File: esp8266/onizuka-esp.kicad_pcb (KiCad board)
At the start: 2 copper layers, 49 x 19 mm, 7 parts, among them P1 FTDI, U1 ESP-01, U2 ESP-12E

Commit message: More faffing
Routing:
- net GND: vias 2 -> 6
- added copper zone on F.Cu, net GND
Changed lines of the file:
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@@
     (thickness 1.6)
     (drawings 4)
-    (tracks 80)
+    (tracks 84)
     (zones 0)
     (modules 7)
@@
       (effects (font (size 1 1) (thickness 0.15)))
     )
-    (fp_text value 100n (at -3.302 0 90) (layer F.SilkS)
+    (fp_text value 100n (at 3.3655 0 90) (layer F.SilkS)
       (effects (font (size 1 1) (thickness 0.15)))
     )
@@
       (effects (font (size 1 1) (thickness 0.15)))
     )
-    (fp_text value FTDI (at 11.41 -1.988 270) (layer F.SilkS)
+    (fp_text value FTDI (at 11.6205 -1.9685 270) (layer F.SilkS) hide
       (effects (font (size 1 1) (thickness 0.15)))
     )
@@
       (effects (font (size 1 1) (thickness 0.15)))
     )
-    (fp_text value 22u (at -2.794 0 90) (layer F.SilkS)
+    (fp_text value 22u (at 2.8575 0.0635 90) (layer F.SilkS)
       (effects (font (size 1 1) (thickness 0.15)))
     )
@@
       (effects (font (size 1 1) (thickness 0.15)))
     )
-    (fp_text value ESP-01 (at 3.81 -1.9685 450) (layer F.SilkS)
+    (fp_text value ESP-01 (at 6.477 4.953 450) (layer F.SilkS)
       (effects (font (size 1 1) (thickness 0.15)))
     )
@@
       (scale (xyz 1 1 1))
       (rotate (xyz 0 0 180))
+    )
+    (model ./esp-01.wrl
+      (at (xyz 0.15 -0.05 0.34))
+      (scale (xyz 1 1 1))
+      (rotate (xyz 0 0 0))
     )
   )
@@
   (gr_line (start 69 37.5) (end 20 37.5) (angle 90) (layer Edge.Cuts) (width 0.15))
   (gr_line (start 69 18.5) (end 69 37.5) (angle 90) (layer Edge.Cuts) (width 0.15))
-  (segment (start 57.9635 32.1945) (end 57.9635 33.7185) (width 0.25) (layer F.Cu) (net 1) (status C00000))
-  (segment (start 57.9635 33.7185) (end 57.9635 32.9685) (width 0.25) (layer F.Cu) (net 1) (status 400000))
+  (via (at 35.5 30) (size 0.6) (drill 0.4) (layers F.Cu B.Cu) (net 1))
+  (via (at 44 21.5) (size 0.6) (drill 0.4) (layers F.Cu B.Cu) (net 1))
+  (via (at 36.5 33.5) (size 0.6) (drill 0.4) (layers F.Cu B.Cu) (net 1))
+  (via (at 52 31) (size 0.6) (drill 0.4) (layers F.Cu B.Cu) (net 1))
+  (segment (start 57.9635 32.1945) (end 57.9635 33.7185) (width 0.25) (layer F.Cu) (net 1))
+  (segment (start 57.9635 33.7185) (end 57.9635 32.9685) (width 0.25) (layer F.Cu) (net 1))
   (segment (start 57.9635 32.9685) (end 57.9755 32.9565) (width 0.25) (layer F.Cu) (net 1))
   (via (at 57.9755 32.9565) (size 0.6) (drill 0.4) (layers F.Cu B.Cu) (net 1))
@@
   (segment (start 29.972 21.59) (end 30.226 21.59) (width 0.25) (layer F.Cu) (net 2))
   (segment (start 29.972 21.59) (end 29.972 21.844) (width 0.25) (layer F.Cu) (net 2))
-  (segment (start 56.4355 35.94) (end 57.7045 34.671) (width 0.25) (layer F.Cu) (net 5) (status 400000))
-  (segment (start 65.1665 34.671) (end 66.4355 35.94) (width 0.25) (layer F.Cu) (net 5) (status 800000))
+  (segment (start 56.4355 35.94) (end 57.7045 34.671) (width 0.25) (layer F.Cu) (net 5))
+  (segment (start 65.1665 34.671) (end 66.4355 35.94) (width 0.25) (layer F.Cu) (net 5))
   (segment (start 57.7045 34.671) (end 65.1665 34.671) (width 0.25) (layer F.Cu) (net 5))
-  (segment (start 56.4355 35.94) (end 56.4635 35.912) (width 0.25) (layer F.Cu) (net 5) (status C00000))
-  (segment (start 56.4635 35.912) (end 56.4635 32.1945) (width 0.25) (layer F.Cu) (net 5) (status C00000))
-  (segment (start 56.4635 32.1945) (end 56.4635 30.9365) (width 0.25) (layer F.Cu) (net 5) (status 400000))
+  (segment (start 56.4355 35.94) (end 56.4635 35.912) (width 0.25) (layer F.Cu) (net 5))
+  (segment (start 56.4635 35.912) (end 56.4635 32.1945) (width 0.25) (layer F.Cu) (net 5))
+  (segment (start 56.4635 32.1945) (end 56.4635 30.9365) (width 0.25) (layer F.Cu) (net 5))
   (segment (start 56.4635 30.9365) (end 53.467 27.94) (width 0.25) (layer F.Cu) (net 5))
   (segment (start 32.512 26.67) (end 33.782 27.94) (width 0.25) (layer F.Cu) (net 5))
@@
       )
     )
+  )
+  (zone (net 1) (net_name GND) (layer F.Cu) (hatch edge 0.508)
+    (connect_pads (clearance 0.3))
+    (min_thickness 0.2)
+    (fill yes (arc_segments 16) (thermal_gap 0.508) (thermal_bridge_width 0.508))
+    (polygon
+      (pts
+        (xy 20 18.5) (xy 69 18.5) (xy 69 37.5) (xy 20 37.5)
+      )
+    )

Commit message: 3d model path correction
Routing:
- net GND: vias 6 -> 2
- net (no net): vias 0 -> 4
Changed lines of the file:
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@@
       (rotate (xyz 0 0 180))
     )
-    (model ./esp-01.wrl
+    (model ${KIPRJMOD}/esp-01.wrl
       (at (xyz 0.15 -0.05 0.34))
       (scale (xyz 1 1 1))
@@
   (gr_line (start 69 37.5) (end 20 37.5) (angle 90) (layer Edge.Cuts) (width 0.15))
   (gr_line (start 69 18.5) (end 69 37.5) (angle 90) (layer Edge.Cuts) (width 0.15))
-  (via (at 35.5 30) (size 0.6) (drill 0.4) (layers F.Cu B.Cu) (net 1))
-  (via (at 44 21.5) (size 0.6) (drill 0.4) (layers F.Cu B.Cu) (net 1))
-  (via (at 36.5 33.5) (size 0.6) (drill 0.4) (layers F.Cu B.Cu) (net 1))
-  (via (at 52 31) (size 0.6) (drill 0.4) (layers F.Cu B.Cu) (net 1))
+  (via (at 35.5 30) (size 0.6) (drill 0.4) (layers F.Cu B.Cu) (net 0))
+  (via (at 44 21.5) (size 0.6) (drill 0.4) (layers F.Cu B.Cu) (net 0))
+  (via (at 36.5 33.5) (size 0.6) (drill 0.4) (layers F.Cu B.Cu) (net 0))
+  (via (at 52 31) (size 0.6) (drill 0.4) (layers F.Cu B.Cu) (net 0))
   (segment (start 57.9635 32.1945) (end 57.9635 33.7185) (width 0.25) (layer F.Cu) (net 1))
   (segment (start 57.9635 33.7185) (end 57.9635 32.9685) (width 0.25) (layer F.Cu) (net 1))

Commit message: Various tweaks
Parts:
- removed P1: FTDI, Socket_Strips:Socket_Strip_Angled_2x06
- added C5: FTDI_CONN, Socket_Strips:Socket_Strip_Angled_2x06, F.Cu at (32.5, 21.6)
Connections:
- U1 pad 3: Net-(U1-Pad3) -> (no net)
- U2 pad 10: Net-(U2-Pad10) -> (no net)
- U2 pad 11: Net-(U2-Pad11) -> (no net)
- U2 pad 12: Net-(U2-Pad12) -> (no net)
- U2 pad 13: Net-(U2-Pad13) -> (no net)
- U2 pad 14: Net-(U2-Pad14) -> (no net)
- U2 pad 16: Net-(U2-Pad16) -> (no net)
- U2 pad 17: Net-(U2-Pad17) -> (no net)
- U2 pad 19: Net-(U2-Pad19) -> (no net)
- U2 pad 2: Net-(U2-Pad2) -> (no net)
- U2 pad 20: Net-(U2-Pad20) -> (no net)
- U2 pad 4: Net-(U2-Pad4) -> (no net)
- U2 pad 5: Net-(U2-Pad5) -> (no net)
- U2 pad 6: Net-(U2-Pad6) -> (no net)
- U2 pad 7: Net-(U2-Pad7) -> (no net)
- U2 pad 9: Net-(U2-Pad9) -> (no net)
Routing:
- net (no net): vias 4 -> 0
- removed copper zone on F.Cu, net GND

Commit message: Add board names revisions and emails.
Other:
- board text added: "Onizuka - ESP V0.1 01/06/16 board@harkonen.net"
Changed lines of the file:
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@@
     (area 19.136999 17.315 69.075001 37.575001)
     (thickness 1.6)
-    (drawings 4)
+    (drawings 5)
     (tracks 84)
     (zones 0)
@@
     )
   )
+  (gr_text "Onizuka - ESP\nV0.1 01/06/16\nboard@harkonen.net" (at 57.785 27.432) (layer B.SilkS)
+    (effects (font (size 1 1) (thickness 0.15)) (justify mirror))
+  )
   (gr_line (start 20 18.5) (end 69 18.5) (angle 90) (layer Edge.Cuts) (width 0.15))

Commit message: Many faffing, new ESP stuff.
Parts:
- removed C5: FTDI_CONN, Socket_Strips:Socket_Strip_Angled_2x06
- added C6: 100n, Capacitors_SMD:C_0603, F.Cu at (37.3, 49.4)
- added C7: 22u, Capacitors_SMD:C_0603, F.Cu at (37.3, 50.9)
- added P1: FTDI_CONN, Pin_Headers:Pin_Header_Angled_2x06, F.Cu at (22.0, 45.0)
- added REF**: MountingHole_2.7mm_M2.5, Mounting_Holes:MountingHole_2.7mm_M2.5, F.Cu at (18.0, 18.0)
- added REF**: MountingHole_2.7mm_M2.5, Mounting_Holes:MountingHole_2.7mm_M2.5, F.Cu at (18.0, 62.0)
- added REF**: MountingHole_2.7mm_M2.5, Mounting_Holes:MountingHole_2.7mm_M2.5, F.Cu at (62.0, 62.0)
- added REF**: MountingHole_2.7mm_M2.5, Mounting_Holes:MountingHole_2.7mm_M2.5, F.Cu at (62.0, 18.0)
- added U3: ESP-02, ESP:ESP-02-Program, F.Cu at (28.5, 56.0)
- U2: footprint esp:ESP-12E -> ESP:ESP-12E-Program
- moved C3 26.6 mm to (57.3, 58.8), turned to 270 degrees
- moved C4 25.1 mm to (58.8, 58.8), turned to 270 degrees
- moved U2 20.7 mm to (50.9, 48.1)
- moved C2 13.4 mm to (36.8, 39.1), turned to 270 degrees
- moved C1 13.2 mm to (35.3, 39.1), turned to 270 degrees
- moved U1 3.93 mm to (37.8, 26.6)
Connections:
- U1 pad 3: (no net) -> Net-(U1-Pad3)
- U2 pad 10: (no net) -> Net-(U2-Pad10)
- U2 pad 11: (no net) -> Net-(U2-Pad11)
- U2 pad 12: (no net) -> Net-(U2-Pad12)
- U2 pad 13: (no net) -> Net-(U2-Pad13)
- U2 pad 14: (no net) -> Net-(U2-Pad14)
- U2 pad 16: (no net) -> Net-(U2-Pad16)
- U2 pad 17: (no net) -> Net-(U2-Pad17)
- U2 pad 19: (no net) -> Net-(U2-Pad19)
- U2 pad 2: (no net) -> Net-(U2-Pad2)
- U2 pad 20: (no net) -> Net-(U2-Pad20)
- U2 pad 4: (no net) -> Net-(U2-Pad4)
- U2 pad 5: (no net) -> Net-(U2-Pad5)
- U2 pad 6: (no net) -> Net-(U2-Pad6)
- U2 pad 7: (no net) -> Net-(U2-Pad7)
- U2 pad 9: (no net) -> Net-(U2-Pad9)
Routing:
- net /DTR: track 43.3 -> 98.1 mm
- net VCC: track 53.9 -> 107.3 mm, vias 2 -> 7
- net /RTS: track 26.1 -> 73.6 mm, vias 1 -> 3
- net /RXD: track 31.9 -> 78.7 mm, vias 1 -> 5
- net /TXD: track 37.9 -> 73.9 mm, vias 0 -> 4
- net GND: track 3.83 -> 0.00 mm, vias 2 -> 0
- added copper zone on F.Cu, net GND
- removed copper zone on B.Cu, net GND
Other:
- board size 49 x 19 mm -> 50 x 50 mm
- rule pad_to_mask_clearance: 0.2 -> 0
- board text added: "ESP-07"

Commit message: Various shuffling, adding farnell part numbers.
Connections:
- P1 pad 10: Net-(P1-Pad10) -> (no net)
- P1 pad 12: /DTR -> (no net)
- P1 pad 2: Net-(P1-Pad2) -> (no net)
- P1 pad 4: Net-(P1-Pad4) -> /DTR
- P1 pad 6: Net-(P1-Pad6) -> (no net)
- P1 pad 8: Net-(P1-Pad8) -> (no net)
- P1 pad 9: Net-(P1-Pad9) -> (no net)
- U1 pad 3: Net-(U1-Pad3) -> (no net)
- U2 pad 10: Net-(U2-Pad10) -> (no net)
- U2 pad 11: Net-(U2-Pad11) -> (no net)
- U2 pad 12: Net-(U2-Pad12) -> (no net)
- U2 pad 13: Net-(U2-Pad13) -> (no net)
- U2 pad 14: Net-(U2-Pad14) -> (no net)
- U2 pad 16: Net-(U2-Pad16) -> (no net)
- U2 pad 17: Net-(U2-Pad17) -> (no net)
- U2 pad 19: Net-(U2-Pad19) -> (no net)
- U2 pad 2: Net-(U2-Pad2) -> (no net)
- U2 pad 20: Net-(U2-Pad20) -> (no net)
- U2 pad 4: Net-(U2-Pad4) -> (no net)
- U2 pad 5: Net-(U2-Pad5) -> (no net)
- U2 pad 6: Net-(U2-Pad6) -> (no net)
- U2 pad 7: Net-(U2-Pad7) -> (no net)
- U2 pad 9: Net-(U2-Pad9) -> (no net)
- U3 pad 7: Net-(U3-Pad7) -> (no net)
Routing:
- net /DTR: track 98.1 -> 87.0 mm

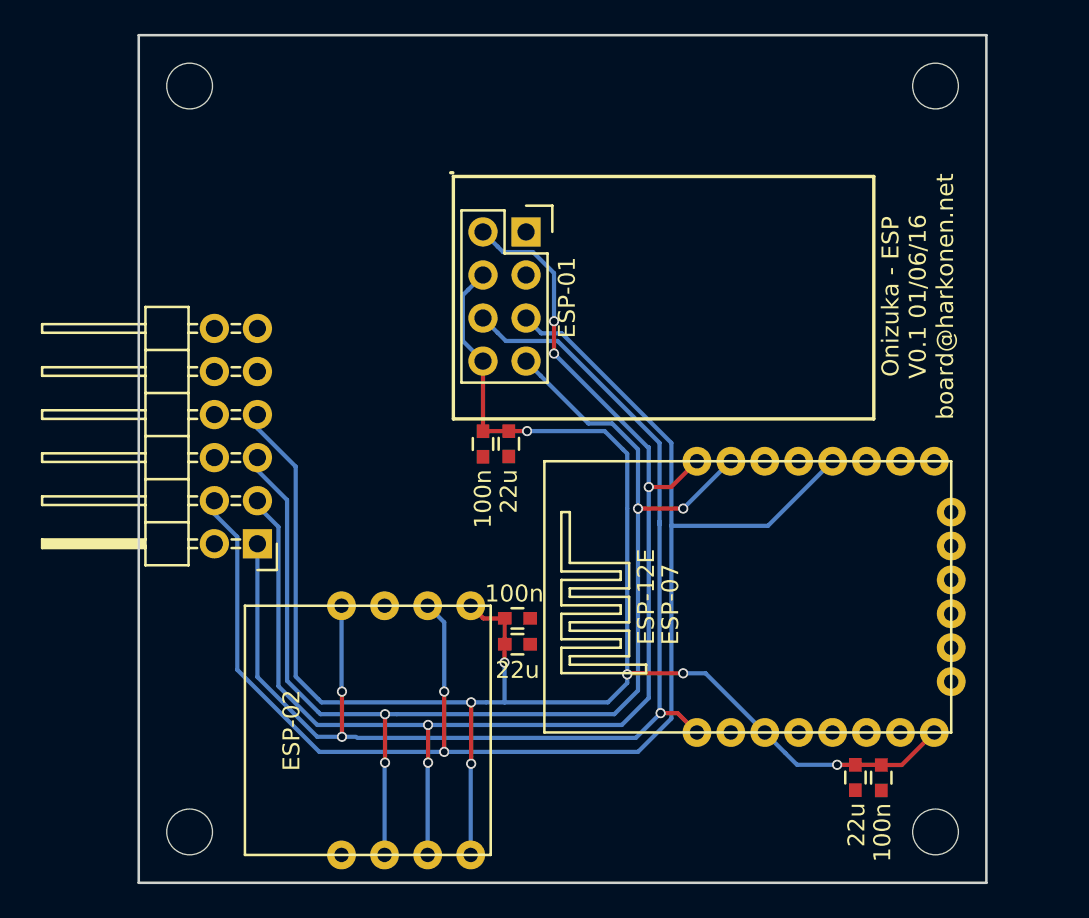
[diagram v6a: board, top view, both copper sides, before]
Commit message: Centre pin header
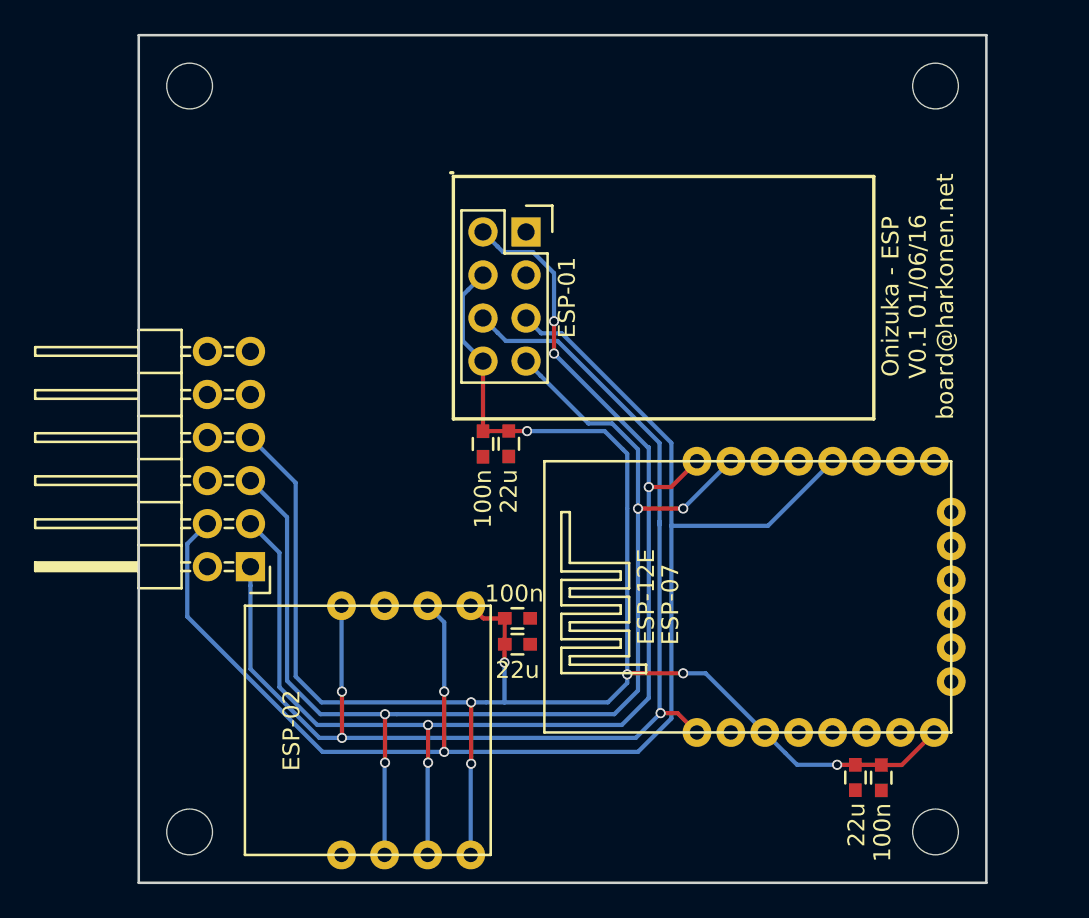
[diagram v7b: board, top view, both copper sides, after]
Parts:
- moved P1 1.42 mm to (21.6, 46.4)
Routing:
- net VCC: track 107.3 -> 106.1 mm
- net /RXD: track 78.7 -> 77.5 mm
- net /TXD: track 73.9 -> 72.7 mm
- net /RTS: track 73.6 -> 72.5 mm
